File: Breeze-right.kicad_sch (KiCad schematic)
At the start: 103 parts, among them J1 J, SW1 CHOCXHSPCB-1U, SW10 CHOCXHSPCB-1U, SW11 CHOCXHSPCB-1U, SW12 CHOCXHSPCB-1U, SW13 CHOCXHSPCB-1U, SW14 CHOCXHSPCB-1U, SW15 CHOCXHSPCB-1U, SW16 CHOCXHSPCB-1U, SW17 CHOCXHSPCB-1U, SW18 CHOCXHSPCB-1U, SW19 CHOCXHSPCB-1U, SW2 CHOCXHSPCB-1U, SW20 CHOCXHSPCB-1U, SW21 CHOCXHSPCB-1U, SW22 CHOCXHSPCB-1U, SW23 CHOCXHSPCB-1U, SW24 CHOCXHSPCB-1U, SW3 CHOCXHSPCB-1U, SW4 CHOCXHSPCB-1U, SW5 CHOCXHSPCB-1U, SW6 CHOCXHSPCB-1U, SW7 CHOCXHSPCB-1U, SW8 CHOCXHSPCB-1U, SW9 CHOCXHSPCB-1U

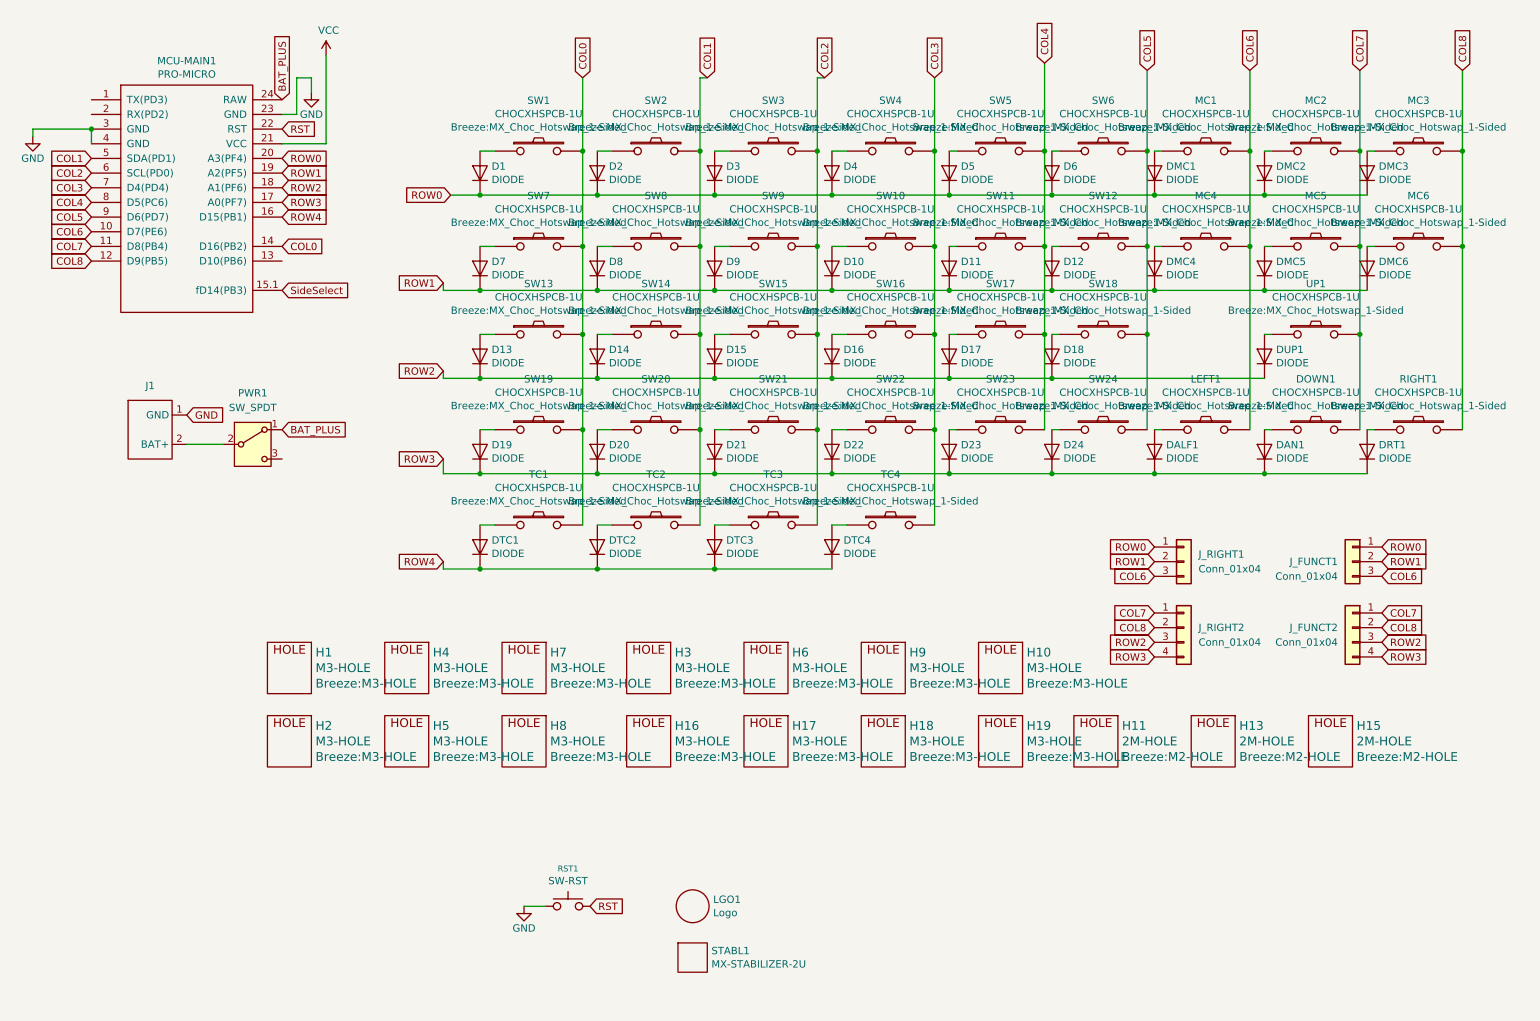
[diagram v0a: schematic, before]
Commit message: redo left PCB, redraw supermini symbol
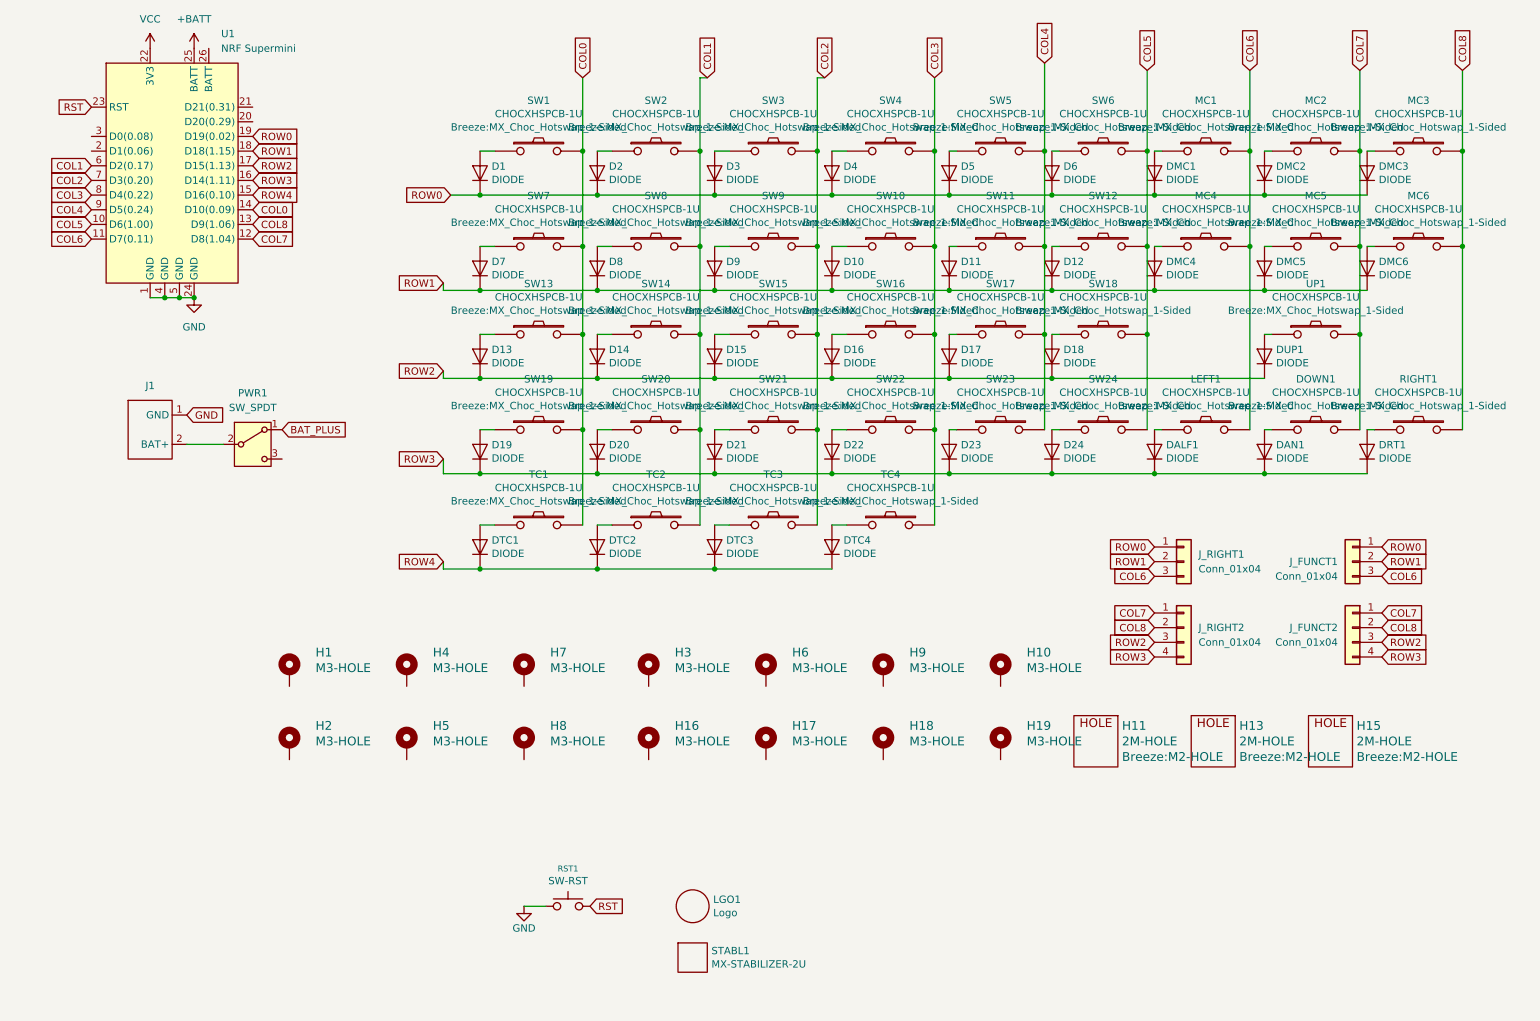
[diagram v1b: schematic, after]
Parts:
- removed MCU-MAIN1: PRO-MICRO, Breeze:ProMicro_1-Sided, symbol Breeze-rescue:ProMicro-Merkaba_Rev0-rescue-Breeze-rescue
- added U1: NRF Supermini, Breeze:NRF_Supermini, symbol Breeze:Pro_Micro
- H1, H10, H16, H17, H18, H19, H2, H3, H4, H5, H6, H7, H8, H9: symbol Breeze-rescue:3M-HOLE-Merkaba_Rev0-rescue-Breeze-rescue -> Mechanical:MountingHole_Pad; now left out of the parts list
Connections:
- net COL0: now also U1.14 (D10(0.09))
- net COL1: now also U1.6 (D2(0.17))
- net COL2: now also U1.7 (D3(0.20))
- net COL3: now also U1.8 (D4(0.22))
- net COL4: now also U1.9 (D5(0.24))
- net COL5: now also U1.10 (D6(1.00))
- net COL6: now also U1.11 (D7(0.11))
- net COL7: now also U1.12 (D8(1.04))
- net COL8: now also U1.13 (D9(1.06))
- net GND: now also U1.1 (GND), U1.24 (GND), U1.4 (GND), U1.5 (GND)
- net ROW0: now also U1.19 (D19(0.02))
- net ROW1: now also U1.18 (D18(1.15))
- net ROW2: now also U1.17 (D15(1.13))
- net ROW3: now also U1.16 (D14(1.11))
- net ROW4: now also U1.15 (D16(0.10))
- net RST: now also U1.23 (RST)
- net VCC: now also U1.22 (3V3)
- new net +BATT: U1.25 (BATT)

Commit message: done
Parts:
- removed H11, H13, H15: 2M-HOLE, Breeze:M2-HOLE, symbol Breeze-rescue:2M-HOLE-Breeze-rescue
- removed H16, H17, H18, H19: M3-HOLE, Breeze:M3-HOLE, symbol Mechanical:MountingHole_Pad
- removed J1: J, Breeze:BATT_PADS, symbol Breeze:BATT_PADS
- removed PWR1: SW_SPDT, Breeze:SS12D00, symbol Switch:SW_SPDT
- added H11, H12, H13, H14: M3, MountingHole:MountingHole_3.2mm_M3_ISO7380_Pad, symbol Mechanical:MountingHole_Pad
- added J1: Conn_01x02, Breeze:BATT_PADS, symbol Connector_Generic:Conn_01x02
- added SW1: SW_SPDT, Breeze:SS12D00, symbol Switch:SW_SPDT
- D1, D2, D3, D4, D5, D6: value DIODE -> 1N4007W; footprint Breeze:SOD-123FL -> Breeze:SOD-123FL_L2.7-W1.8-LS3.7-RD; symbol Breeze-rescue:Diode-cache-Merkaba_Rev0-rescue-Breeze-rescue -> Diode:1N4007
- D10: renamed from D7; value DIODE -> 1N4007W; footprint Breeze:SOD-123FL -> Breeze:SOD-123FL_L2.7-W1.8-LS3.7-RD; symbol Breeze-rescue:Diode-cache-Merkaba_Rev0-rescue-Breeze-rescue -> Diode:1N4007
- D11: renamed from D8; value DIODE -> 1N4007W; footprint Breeze:SOD-123FL -> Breeze:SOD-123FL_L2.7-W1.8-LS3.7-RD; symbol Breeze-rescue:Diode-cache-Merkaba_Rev0-rescue-Breeze-rescue -> Diode:1N4007
- D12: renamed from D9; value DIODE -> 1N4007W; footprint Breeze:SOD-123FL -> Breeze:SOD-123FL_L2.7-W1.8-LS3.7-RD; symbol Breeze-rescue:Diode-cache-Merkaba_Rev0-rescue-Breeze-rescue -> Diode:1N4007
- D13: renamed from D10; value DIODE -> 1N4007W; footprint Breeze:SOD-123FL -> Breeze:SOD-123FL_L2.7-W1.8-LS3.7-RD; symbol Breeze-rescue:Diode-cache-Merkaba_Rev0-rescue-Breeze-rescue -> Diode:1N4007
- D14: renamed from D11; value DIODE -> 1N4007W; footprint Breeze:SOD-123FL -> Breeze:SOD-123FL_L2.7-W1.8-LS3.7-RD; symbol Breeze-rescue:Diode-cache-Merkaba_Rev0-rescue-Breeze-rescue -> Diode:1N4007
- D15: renamed from D12; value DIODE -> 1N4007W; footprint Breeze:SOD-123FL -> Breeze:SOD-123FL_L2.7-W1.8-LS3.7-RD; symbol Breeze-rescue:Diode-cache-Merkaba_Rev0-rescue-Breeze-rescue -> Diode:1N4007
- D16: renamed from DMC4; value DIODE -> 1N4007W; footprint Breeze:SOD-123FL -> Breeze:SOD-123FL_L2.7-W1.8-LS3.7-RD; symbol Breeze-rescue:Diode-cache-Merkaba_Rev0-rescue-Breeze-rescue -> Diode:1N4007
- D17: renamed from DMC5; value DIODE -> 1N4007W; footprint Breeze:SOD-123FL -> Breeze:SOD-123FL_L2.7-W1.8-LS3.7-RD; symbol Breeze-rescue:Diode-cache-Merkaba_Rev0-rescue-Breeze-rescue -> Diode:1N4007
- D18: renamed from DMC6; value DIODE -> 1N4007W; footprint Breeze:SOD-123FL -> Breeze:SOD-123FL_L2.7-W1.8-LS3.7-RD; symbol Breeze-rescue:Diode-cache-Merkaba_Rev0-rescue-Breeze-rescue -> Diode:1N4007
- D19: renamed from D13; value DIODE -> 1N4007W; footprint Breeze:SOD-123FL -> Breeze:SOD-123FL_L2.7-W1.8-LS3.7-RD; symbol Breeze-rescue:Diode-cache-Merkaba_Rev0-rescue-Breeze-rescue -> Diode:1N4007
- D20: renamed from D14; value DIODE -> 1N4007W; footprint Breeze:SOD-123FL -> Breeze:SOD-123FL_L2.7-W1.8-LS3.7-RD; symbol Breeze-rescue:Diode-cache-Merkaba_Rev0-rescue-Breeze-rescue -> Diode:1N4007
- D21: renamed from D15; value DIODE -> 1N4007W; footprint Breeze:SOD-123FL -> Breeze:SOD-123FL_L2.7-W1.8-LS3.7-RD; symbol Breeze-rescue:Diode-cache-Merkaba_Rev0-rescue-Breeze-rescue -> Diode:1N4007
- D22: renamed from D16; value DIODE -> 1N4007W; footprint Breeze:SOD-123FL -> Breeze:SOD-123FL_L2.7-W1.8-LS3.7-RD; symbol Breeze-rescue:Diode-cache-Merkaba_Rev0-rescue-Breeze-rescue -> Diode:1N4007
- D23: renamed from D17; value DIODE -> 1N4007W; footprint Breeze:SOD-123FL -> Breeze:SOD-123FL_L2.7-W1.8-LS3.7-RD; symbol Breeze-rescue:Diode-cache-Merkaba_Rev0-rescue-Breeze-rescue -> Diode:1N4007
- D24: renamed from D18; value DIODE -> 1N4007W; footprint Breeze:SOD-123FL -> Breeze:SOD-123FL_L2.7-W1.8-LS3.7-RD; symbol Breeze-rescue:Diode-cache-Merkaba_Rev0-rescue-Breeze-rescue -> Diode:1N4007
- D25: renamed from DUP1; value DIODE -> 1N4007W; footprint Breeze:SOD-123FL -> Breeze:SOD-123FL_L2.7-W1.8-LS3.7-RD; symbol Breeze-rescue:Diode-cache-Merkaba_Rev0-rescue-Breeze-rescue -> Diode:1N4007
- D26: renamed from D19; value DIODE -> 1N4007W; footprint Breeze:SOD-123FL -> Breeze:SOD-123FL_L2.7-W1.8-LS3.7-RD; symbol Breeze-rescue:Diode-cache-Merkaba_Rev0-rescue-Breeze-rescue -> Diode:1N4007
- D27: renamed from D20; value DIODE -> 1N4007W; footprint Breeze:SOD-123FL -> Breeze:SOD-123FL_L2.7-W1.8-LS3.7-RD; symbol Breeze-rescue:Diode-cache-Merkaba_Rev0-rescue-Breeze-rescue -> Diode:1N4007
- D28: renamed from D21; value DIODE -> 1N4007W; footprint Breeze:SOD-123FL -> Breeze:SOD-123FL_L2.7-W1.8-LS3.7-RD; symbol Breeze-rescue:Diode-cache-Merkaba_Rev0-rescue-Breeze-rescue -> Diode:1N4007
- D29: renamed from D22; value DIODE -> 1N4007W; footprint Breeze:SOD-123FL -> Breeze:SOD-123FL_L2.7-W1.8-LS3.7-RD; symbol Breeze-rescue:Diode-cache-Merkaba_Rev0-rescue-Breeze-rescue -> Diode:1N4007
- D30: renamed from D23; value DIODE -> 1N4007W; footprint Breeze:SOD-123FL -> Breeze:SOD-123FL_L2.7-W1.8-LS3.7-RD; symbol Breeze-rescue:Diode-cache-Merkaba_Rev0-rescue-Breeze-rescue -> Diode:1N4007
- D31: renamed from D24; value DIODE -> 1N4007W; footprint Breeze:SOD-123FL -> Breeze:SOD-123FL_L2.7-W1.8-LS3.7-RD; symbol Breeze-rescue:Diode-cache-Merkaba_Rev0-rescue-Breeze-rescue -> Diode:1N4007
- D32: renamed from DALF1; value DIODE -> 1N4007W; footprint Breeze:SOD-123FL -> Breeze:SOD-123FL_L2.7-W1.8-LS3.7-RD; symbol Breeze-rescue:Diode-cache-Merkaba_Rev0-rescue-Breeze-rescue -> Diode:1N4007
- D33: renamed from DAN1; value DIODE -> 1N4007W; footprint Breeze:SOD-123FL -> Breeze:SOD-123FL_L2.7-W1.8-LS3.7-RD; symbol Breeze-rescue:Diode-cache-Merkaba_Rev0-rescue-Breeze-rescue -> Diode:1N4007
- D34: renamed from DRT1; value DIODE -> 1N4007W; footprint Breeze:SOD-123FL -> Breeze:SOD-123FL_L2.7-W1.8-LS3.7-RD; symbol Breeze-rescue:Diode-cache-Merkaba_Rev0-rescue-Breeze-rescue -> Diode:1N4007
- D35: renamed from DTC1; value DIODE -> 1N4007W; footprint Breeze:SOD-123FL -> Breeze:SOD-123FL_L2.7-W1.8-LS3.7-RD; symbol Breeze-rescue:Diode-cache-Merkaba_Rev0-rescue-Breeze-rescue -> Diode:1N4007
- D36: renamed from DTC2; value DIODE -> 1N4007W; footprint Breeze:SOD-123FL -> Breeze:SOD-123FL_L2.7-W1.8-LS3.7-RD; symbol Breeze-rescue:Diode-cache-Merkaba_Rev0-rescue-Breeze-rescue -> Diode:1N4007
- D37: renamed from DTC3; value DIODE -> 1N4007W; footprint Breeze:SOD-123FL -> Breeze:SOD-123FL_L2.7-W1.8-LS3.7-RD; symbol Breeze-rescue:Diode-cache-Merkaba_Rev0-rescue-Breeze-rescue -> Diode:1N4007
- D38: renamed from DTC4; value DIODE -> 1N4007W; footprint Breeze:SOD-123FL -> Breeze:SOD-123FL_L2.7-W1.8-LS3.7-RD; symbol Breeze-rescue:Diode-cache-Merkaba_Rev0-rescue-Breeze-rescue -> Diode:1N4007
- D7: renamed from DMC1; value DIODE -> 1N4007W; footprint Breeze:SOD-123FL -> Breeze:SOD-123FL_L2.7-W1.8-LS3.7-RD; symbol Breeze-rescue:Diode-cache-Merkaba_Rev0-rescue-Breeze-rescue -> Diode:1N4007
- D8: renamed from DMC2; value DIODE -> 1N4007W; footprint Breeze:SOD-123FL -> Breeze:SOD-123FL_L2.7-W1.8-LS3.7-RD; symbol Breeze-rescue:Diode-cache-Merkaba_Rev0-rescue-Breeze-rescue -> Diode:1N4007
- D9: renamed from DMC3; value DIODE -> 1N4007W; footprint Breeze:SOD-123FL -> Breeze:SOD-123FL_L2.7-W1.8-LS3.7-RD; symbol Breeze-rescue:Diode-cache-Merkaba_Rev0-rescue-Breeze-rescue -> Diode:1N4007
- G1: renamed from LGO1; symbol Breeze-rescue:Logo-Breeze-rescue -> Mechanical:MountingHole; now left out of the parts list
- H1, H10, H3, H4, H6, H7, H9: value M3-HOLE -> M3; footprint Breeze:M3-HOLE -> MountingHole:MountingHole_3.2mm_M3_ISO7380_Pad
- H18: renamed from STABL1; symbol Breeze-rescue:MX-STABILIZER-2U-Merkaba_Rev0-rescue-Breeze-rescue -> Mechanical:MountingHole; now left out of the parts list
- H2, H5, H8: value M3-HOLE -> M3; footprint Breeze:M3-HOLE -> MountingHole:MountingHole_3.2mm_M3_ISO7380_Pad_TopOnly
- UPXS1: renamed from UP1; symbol Breeze-rescue:CHOCXHSPCB-1U-cache-Merkaba_Rev0-rescue-Breeze-rescue -> Switch:SW_Push
- XS1: renamed from SW1; symbol Breeze-rescue:CHOCXHSPCB-1U-cache-Merkaba_Rev0-rescue-Breeze-rescue -> Switch:SW_Push
- XS10: renamed from SW7; symbol Breeze-rescue:CHOCXHSPCB-1U-cache-Merkaba_Rev0-rescue-Breeze-rescue -> Switch:SW_Push
- XS11: renamed from SW8; symbol Breeze-rescue:CHOCXHSPCB-1U-cache-Merkaba_Rev0-rescue-Breeze-rescue -> Switch:SW_Push
- XS12: renamed from SW9; symbol Breeze-rescue:CHOCXHSPCB-1U-cache-Merkaba_Rev0-rescue-Breeze-rescue -> Switch:SW_Push
- XS13: renamed from SW10; symbol Breeze-rescue:CHOCXHSPCB-1U-cache-Merkaba_Rev0-rescue-Breeze-rescue -> Switch:SW_Push
- XS14: renamed from SW11; symbol Breeze-rescue:CHOCXHSPCB-1U-cache-Merkaba_Rev0-rescue-Breeze-rescue -> Switch:SW_Push
- XS15: renamed from SW12; symbol Breeze-rescue:CHOCXHSPCB-1U-cache-Merkaba_Rev0-rescue-Breeze-rescue -> Switch:SW_Push
- XS16: renamed from MC4; symbol Breeze-rescue:CHOCXHSPCB-1U-cache-Merkaba_Rev0-rescue-Breeze-rescue -> Switch:SW_Push
- XS17: renamed from MC5; symbol Breeze-rescue:CHOCXHSPCB-1U-cache-Merkaba_Rev0-rescue-Breeze-rescue -> Switch:SW_Push
- XS18: renamed from MC6; symbol Breeze-rescue:CHOCXHSPCB-1U-cache-Merkaba_Rev0-rescue-Breeze-rescue -> Switch:SW_Push
- XS19: renamed from SW13; symbol Breeze-rescue:CHOCXHSPCB-1U-cache-Merkaba_Rev0-rescue-Breeze-rescue -> Switch:SW_Push
- XS2: renamed from SW2; symbol Breeze-rescue:CHOCXHSPCB-1U-cache-Merkaba_Rev0-rescue-Breeze-rescue -> Switch:SW_Push
- XS20: renamed from SW14; symbol Breeze-rescue:CHOCXHSPCB-1U-cache-Merkaba_Rev0-rescue-Breeze-rescue -> Switch:SW_Push
- XS21: renamed from SW15; symbol Breeze-rescue:CHOCXHSPCB-1U-cache-Merkaba_Rev0-rescue-Breeze-rescue -> Switch:SW_Push
- XS22: renamed from SW16; symbol Breeze-rescue:CHOCXHSPCB-1U-cache-Merkaba_Rev0-rescue-Breeze-rescue -> Switch:SW_Push
- XS23: renamed from SW17; symbol Breeze-rescue:CHOCXHSPCB-1U-cache-Merkaba_Rev0-rescue-Breeze-rescue -> Switch:SW_Push
- XS24: renamed from SW18; symbol Breeze-rescue:CHOCXHSPCB-1U-cache-Merkaba_Rev0-rescue-Breeze-rescue -> Switch:SW_Push
- XS25: renamed from SW19; symbol Breeze-rescue:CHOCXHSPCB-1U-cache-Merkaba_Rev0-rescue-Breeze-rescue -> Switch:SW_Push
- XS26: renamed from SW20; symbol Breeze-rescue:CHOCXHSPCB-1U-cache-Merkaba_Rev0-rescue-Breeze-rescue -> Switch:SW_Push
- XS27: renamed from SW21; symbol Breeze-rescue:CHOCXHSPCB-1U-cache-Merkaba_Rev0-rescue-Breeze-rescue -> Switch:SW_Push
- XS28: renamed from SW22; symbol Breeze-rescue:CHOCXHSPCB-1U-cache-Merkaba_Rev0-rescue-Breeze-rescue -> Switch:SW_Push
- XS29: renamed from SW23; symbol Breeze-rescue:CHOCXHSPCB-1U-cache-Merkaba_Rev0-rescue-Breeze-rescue -> Switch:SW_Push
- XS3: renamed from SW3; symbol Breeze-rescue:CHOCXHSPCB-1U-cache-Merkaba_Rev0-rescue-Breeze-rescue -> Switch:SW_Push
- XS30: renamed from SW24; symbol Breeze-rescue:CHOCXHSPCB-1U-cache-Merkaba_Rev0-rescue-Breeze-rescue -> Switch:SW_Push
- XS31: renamed from LEFT1; symbol Breeze-rescue:CHOCXHSPCB-1U-cache-Merkaba_Rev0-rescue-Breeze-rescue -> Switch:SW_Push
- XS32: renamed from DOWN1; symbol Breeze-rescue:CHOCXHSPCB-1U-cache-Merkaba_Rev0-rescue-Breeze-rescue -> Switch:SW_Push
- XS33: renamed from RIGHT1; symbol Breeze-rescue:CHOCXHSPCB-1U-cache-Merkaba_Rev0-rescue-Breeze-rescue -> Switch:SW_Push
- XS34: renamed from TC1; symbol Breeze-rescue:CHOCXHSPCB-1U-cache-Merkaba_Rev0-rescue-Breeze-rescue -> Switch:SW_Push
- XS35: renamed from TC2; symbol Breeze-rescue:CHOCXHSPCB-1U-cache-Merkaba_Rev0-rescue-Breeze-rescue -> Switch:SW_Push
- XS36: renamed from TC3; symbol Breeze-rescue:CHOCXHSPCB-1U-cache-Merkaba_Rev0-rescue-Breeze-rescue -> Switch:SW_Push
- XS37: renamed from TC4; symbol Breeze-rescue:CHOCXHSPCB-1U-cache-Merkaba_Rev0-rescue-Breeze-rescue -> Switch:SW_Push
- XS4: renamed from SW4; symbol Breeze-rescue:CHOCXHSPCB-1U-cache-Merkaba_Rev0-rescue-Breeze-rescue -> Switch:SW_Push
- XS5: renamed from SW5; symbol Breeze-rescue:CHOCXHSPCB-1U-cache-Merkaba_Rev0-rescue-Breeze-rescue -> Switch:SW_Push
- XS6: renamed from SW6; symbol Breeze-rescue:CHOCXHSPCB-1U-cache-Merkaba_Rev0-rescue-Breeze-rescue -> Switch:SW_Push
- XS7: renamed from MC1; symbol Breeze-rescue:CHOCXHSPCB-1U-cache-Merkaba_Rev0-rescue-Breeze-rescue -> Switch:SW_Push
- XS8: renamed from MC2; symbol Breeze-rescue:CHOCXHSPCB-1U-cache-Merkaba_Rev0-rescue-Breeze-rescue -> Switch:SW_Push
- XS9: renamed from MC3; symbol Breeze-rescue:CHOCXHSPCB-1U-cache-Merkaba_Rev0-rescue-Breeze-rescue -> Switch:SW_Push
- renumbered J_RIGHT1 to J2, J_FUNCT1 to J3, J_RIGHT2 to J4, J_FUNCT2 to J5, RST1 to SW2
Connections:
- net +BATT: now also SW1.1 (A)
- net GND: now also H1.1, H10.1, H2.1, H3.1, H4.1, H5.1, H6.1, H7.1, H8.1, H9.1, H11.1, H12.1, H13.1, H14.1, J1.1 (Pin_1)
- new net: J1.2 (Pin_2), SW1.2 (B)
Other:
- moved on the sheet: D1, D10, D11, D12, D13, D14, D15, D16, D17, D18, D19, D2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

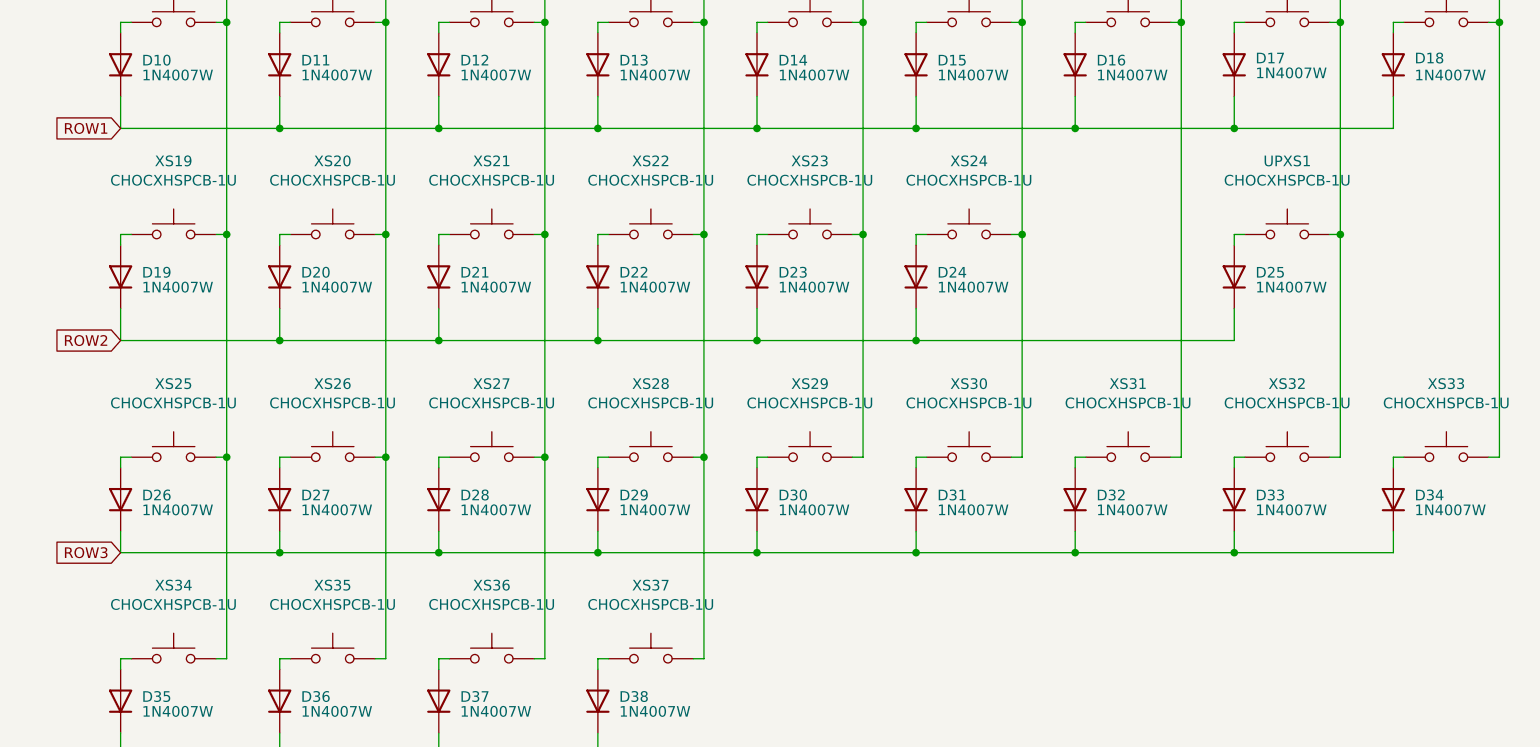
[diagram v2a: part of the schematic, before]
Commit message: fix mis-named component(xs25)
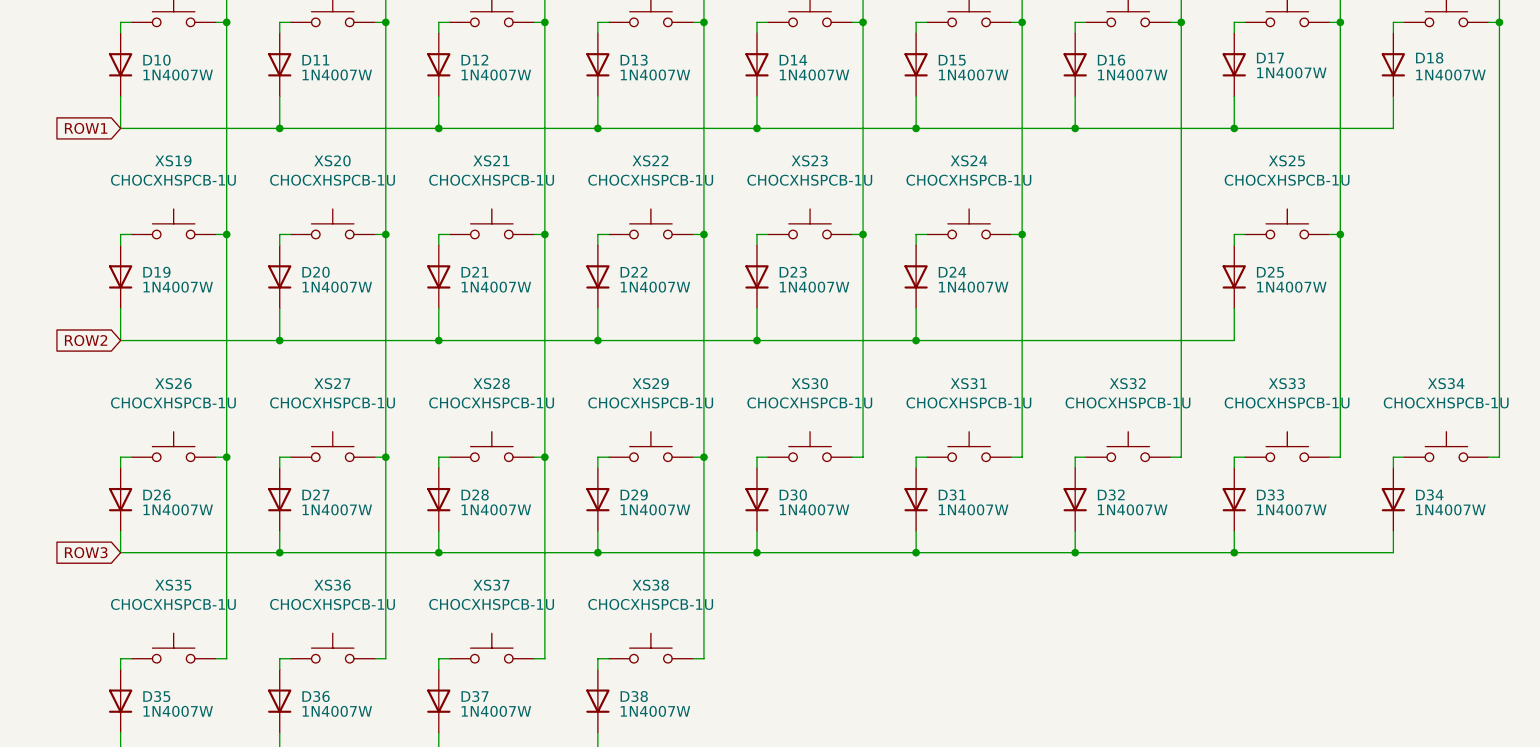
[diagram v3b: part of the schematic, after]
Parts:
- renumbered UPXS1 to XS25, XS25 to XS26, XS26 to XS27, XS27 to XS28, XS28 to XS29, XS29 to XS30, XS30 to XS31, XS31 to XS32, XS32 to XS33, XS33 to XS34, XS34 to XS35, XS35 to XS36, XS36 to XS37, XS37 to XS38
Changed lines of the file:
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@@
 		(on_board yes)
 		(dnp no)
-		(property "Reference" "UPXS1"
+		(property "Reference" "XS25"
 			(at 254 80.137 0)
 			(effects
@@
 			(project "Breeze-right"
 				(path "/e63e39d7-6ac0-4ffd-8aa3-1841a4541b55"
-					(reference "UPXS1")
+					(reference "XS25")
 					(unit 1)
 				)
@@
 		(on_board yes)
 		(dnp no)
-		(property "Reference" "XS25"
+		(property "Reference" "XS26"
 			(at 120.65 106.807 0)
 			(effects
@@
 			(project "Breeze-right"
 				(path "/e63e39d7-6ac0-4ffd-8aa3-1841a4541b55"
-					(reference "XS25")
+					(reference "XS26")
 					(unit 1)
 				)
@@
 		(on_board yes)
 		(dnp no)
-		(property "Reference" "XS26"
+		(property "Reference" "XS27"
 			(at 139.7 106.807 0)
 			(effects
@@
 			(project "Breeze-right"
 				(path "/e63e39d7-6ac0-4ffd-8aa3-1841a4541b55"
-					(reference "XS26")
+					(reference "XS27")
 					(unit 1)
 				)
@@
 		(on_board yes)
 		(dnp no)
-		(property "Reference" "XS27"
+		(property "Reference" "XS28"
 			(at 158.75 106.807 0)
 			(effects
@@
 			(project "Breeze-right"
 				(path "/e63e39d7-6ac0-4ffd-8aa3-1841a4541b55"
-					(reference "XS27")
+					(reference "XS28")
 					(unit 1)
 				)
@@
 		(on_board yes)
 		(dnp no)
-		(property "Reference" "XS28"
+		(property "Reference" "XS29"
 			(at 177.8 106.807 0)
 			(effects
@@
 			(project "Breeze-right"
 				(path "/e63e39d7-6ac0-4ffd-8aa3-1841a4541b55"
-					(reference "XS28")
+					(reference "XS29")
 					(unit 1)
 				)
@@
 		(on_board yes)
 		(dnp no)
-		(property "Reference" "XS29"
+		(property "Reference" "XS30"
 			(at 196.85 106.807 0)
 			(effects
@@
 			(project "Breeze-right"
 				(path "/e63e39d7-6ac0-4ffd-8aa3-1841a4541b55"
-					(reference "XS29")
+					(reference "XS30")
 					(unit 1)
 				)
@@
 		(on_board yes)
 		(dnp no)
-		(property "Reference" "XS30"
+		(property "Reference" "XS31"
 			(at 215.9 106.807 0)
 			(effects
@@
 			(project "Breeze-right"
 				(path "/e63e39d7-6ac0-4ffd-8aa3-1841a4541b55"
-					(reference "XS30")
+					(reference "XS31")
 					(unit 1)
 				)
@@
 		(on_board yes)
 		(dnp no)
-		(property "Reference" "XS31"
+		(property "Reference" "XS32"
 			(at 234.95 106.807 0)
 			(effects
@@
 			(project "Breeze-right"
 				(path "/e63e39d7-6ac0-4ffd-8aa3-1841a4541b55"
-					(reference "XS31")
+					(reference "XS32")
 					(unit 1)
 				)
@@
 		(on_board yes)
 		(dnp no)
-		(property "Reference" "XS32"
+		(property "Reference" "XS33"
 			(at 254 106.807 0)
 			(effects
@@
 			(project "Breeze-right"
 				(path "/e63e39d7-6ac0-4ffd-8aa3-1841a4541b55"
-					(reference "XS32")
+					(reference "XS33")
 					(unit 1)
 				)
@@
 		(on_board yes)
 		(dnp no)
-		(property "Reference" "XS33"
+		(property "Reference" "XS34"
 			(at 273.05 106.807 0)
 			(effects
@@
 			(project "Breeze-right"
 				(path "/e63e39d7-6ac0-4ffd-8aa3-1841a4541b55"
-					(reference "XS33")
+					(reference "XS34")
 					(unit 1)
 				)
@@
 		(on_board yes)
 		(dnp no)
-		(property "Reference" "XS34"
+		(property "Reference" "XS35"
 			(at 120.65 130.937 0)
 			(effects
@@
 			(project "Breeze-right"
 				(path "/e63e39d7-6ac0-4ffd-8aa3-1841a4541b55"
-					(reference "XS34")
+					(reference "XS35")
 					(unit 1)
 				)
@@
 		(on_board yes)
 		(dnp no)
-		(property "Reference" "XS35"
+		(property "Reference" "XS36"
 			(at 139.7 130.937 0)
 			(effects
@@
 			(project "Breeze-right"
 				(path "/e63e39d7-6ac0-4ffd-8aa3-1841a4541b55"
-					(reference "XS35")
+					(reference "XS36")
 					(unit 1)
 				)
@@
 		(on_board yes)
 		(dnp no)
-		(property "Reference" "XS36"
+		(property "Reference" "XS37"
 			(at 158.75 130.937 0)
 			(effects
@@
 			(project "Breeze-right"
 				(path "/e63e39d7-6ac0-4ffd-8aa3-1841a4541b55"
-					(reference "XS36")
+					(reference "XS37")
 					(unit 1)
 				)
@@
 		(on_board yes)
 		(dnp no)
-		(property "Reference" "XS37"
+		(property "Reference" "XS38"
 			(at 177.8 130.937 0)
 			(effects
@@
 			(project "Breeze-right"
 				(path "/e63e39d7-6ac0-4ffd-8aa3-1841a4541b55"
-					(reference "XS37")
-					(unit 1)
-				)
+					(reference "XS38")
+					(unit 1)
+				)
